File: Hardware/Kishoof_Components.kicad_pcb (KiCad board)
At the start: 2 copper layers, 47 parts, among them U1 STM32H7B0VBTx, U3 TPS561201, U4 LT1117-3.3, U5 TL074, U6 MX25LM51245G

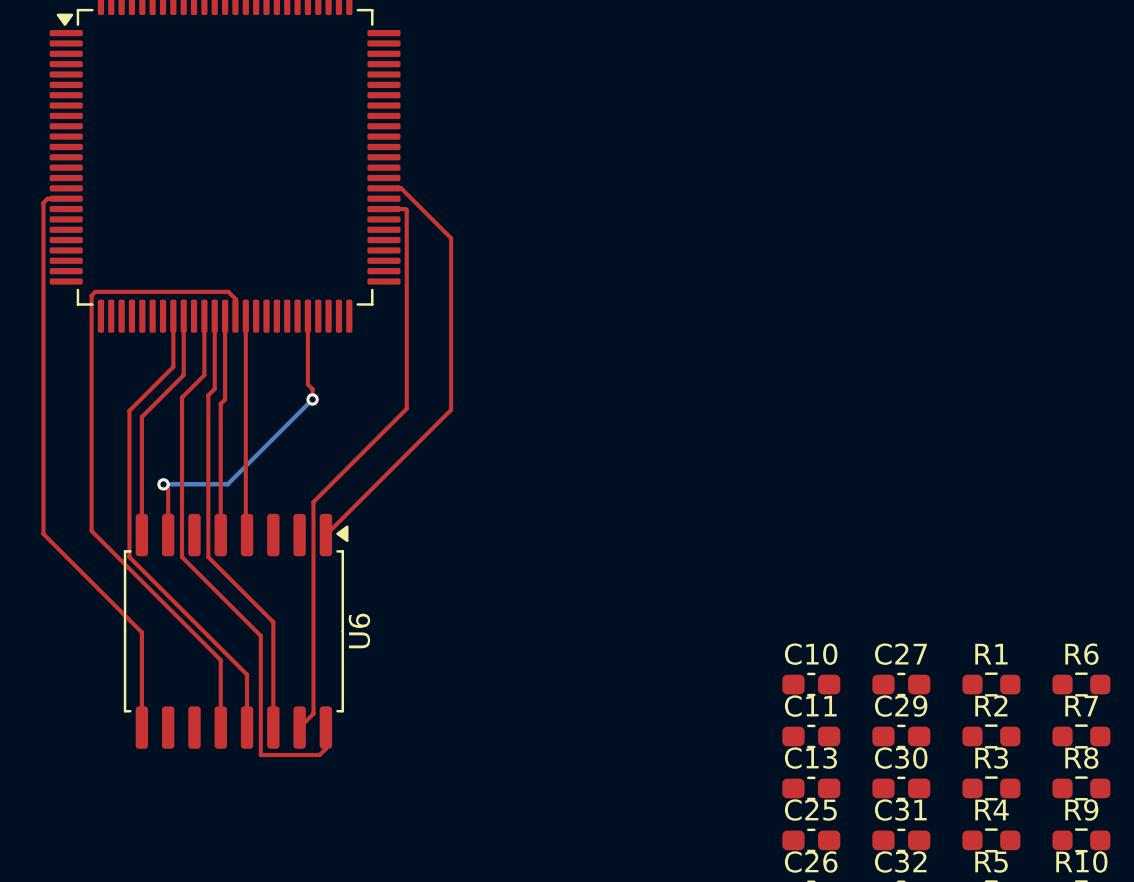
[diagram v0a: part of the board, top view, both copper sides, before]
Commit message: Additional schematic layout
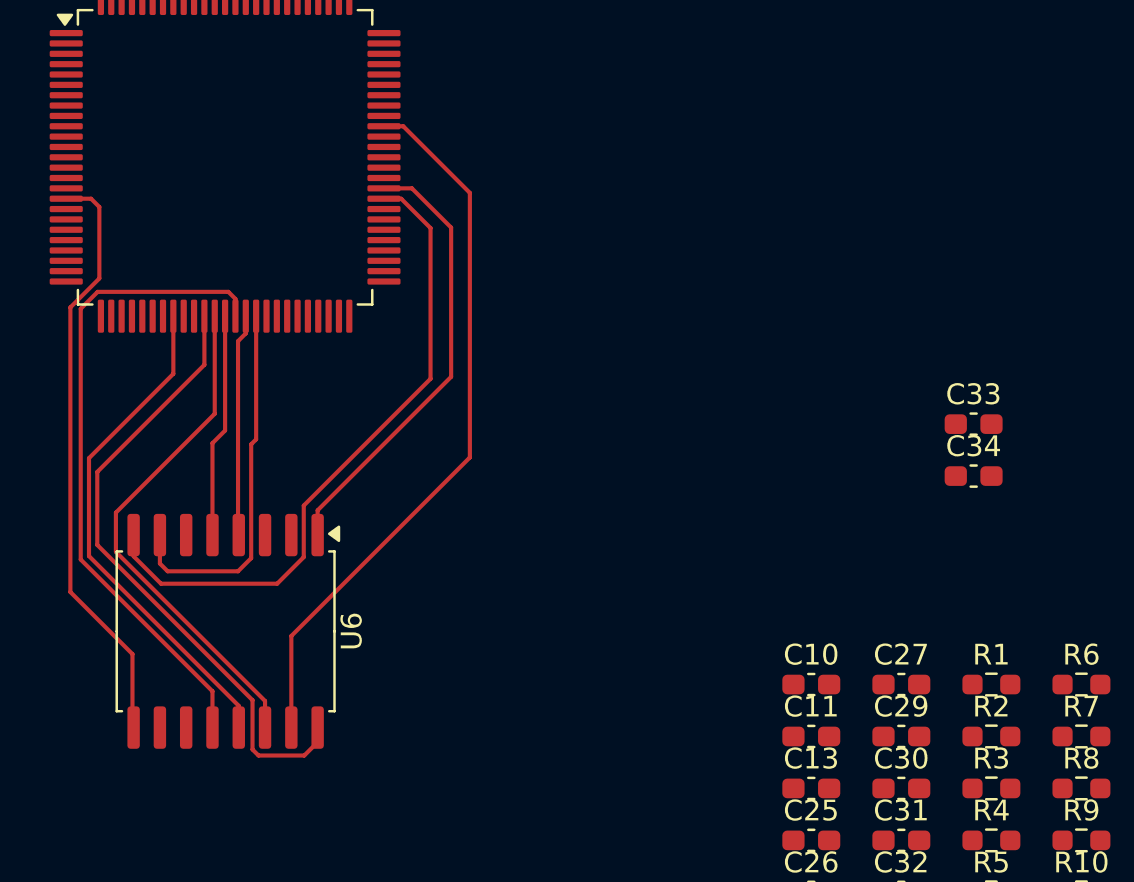
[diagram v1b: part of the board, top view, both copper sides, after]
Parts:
- added C33: 100nF, Capacitor_SMD:C_0603_1608Metric_Pad1.08x0.95mm_HandSolder, F.Cu at (78.9, 71.3)
- added C34: 100nF, Capacitor_SMD:C_0603_1608Metric_Pad1.08x0.95mm_HandSolder, F.Cu at (78.9, 73.8)
- moved U6 0.40 mm to (42.8, 81.3)
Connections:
- U1 pad 1: /OCTOSPIM_P1_IO2 -> unconnected-(U1-PE2-Pad1)
- U1 pad 18: /OCTOSPIM_P1_IO0 -> unconnected-(U1-PC3_C-Pad18)
- U1 pad 23: /OCTOSPIM_P1_DQS -> unconnected-(U1-PA1-Pad23)
- U1 pad 30: /OCTOSPIM_P1_IO3 -> unconnected-(U1-PA6-Pad30)
- U1 pad 34: /OCTOSPIM_P1_IO1 -> unconnected-(U1-PB0-Pad34)
- U1 pad 41: unconnected-(U1-PE11-Pad41) -> /OCTOSPIM_P1_NCS
- U1 pad 58: /OCTOSPIM_P1_IO0 -> unconnected-(U1-PD11-Pad58)
- U1 pad 85: /OCTOSPIM_P1_IO4 -> unconnected-(U1-PD4-Pad85)
- U1 pad 86: /OCTOSPIM_P1_IO5 -> unconnected-(U1-PD5-Pad86)
- U1 pad 87: /OCTOSPIM_P1_IO6 -> unconnected-(U1-PD6-Pad87)
- U1 pad 88: /OCTOSPIM_P1_IO7 -> unconnected-(U1-PD7-Pad88)
- U6 pad 10: unconnected-(U6-GND-Pad10) -> GND
- U6 pad 11: unconnected-(U6-VCC-Pad11) -> +3V3
- U6 pad 2: unconnected-(U6-VCC-Pad2) -> +3V3
- U6 pad 6: unconnected-(U6-GND-Pad6) -> GND
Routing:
- net /OCTOSPIM_P1_IO1: track 11.4 -> 31.6 mm
- net /OCTOSPIM_P1_IO0: track 28.3 -> 34.9 mm
- net /OCTOSPIM_P1_IO4: track 21.3 -> 24.8 mm
- net /OCTOSPIM_P1_CLK: track 27.5 -> 30.4 mm
- net /OCTOSPIM_P1_NCS: track 15.6 -> 18.0 mm, vias 2 -> 0
- net /OCTOSPIM_P1_DQS: track 23.1 -> 24.6 mm

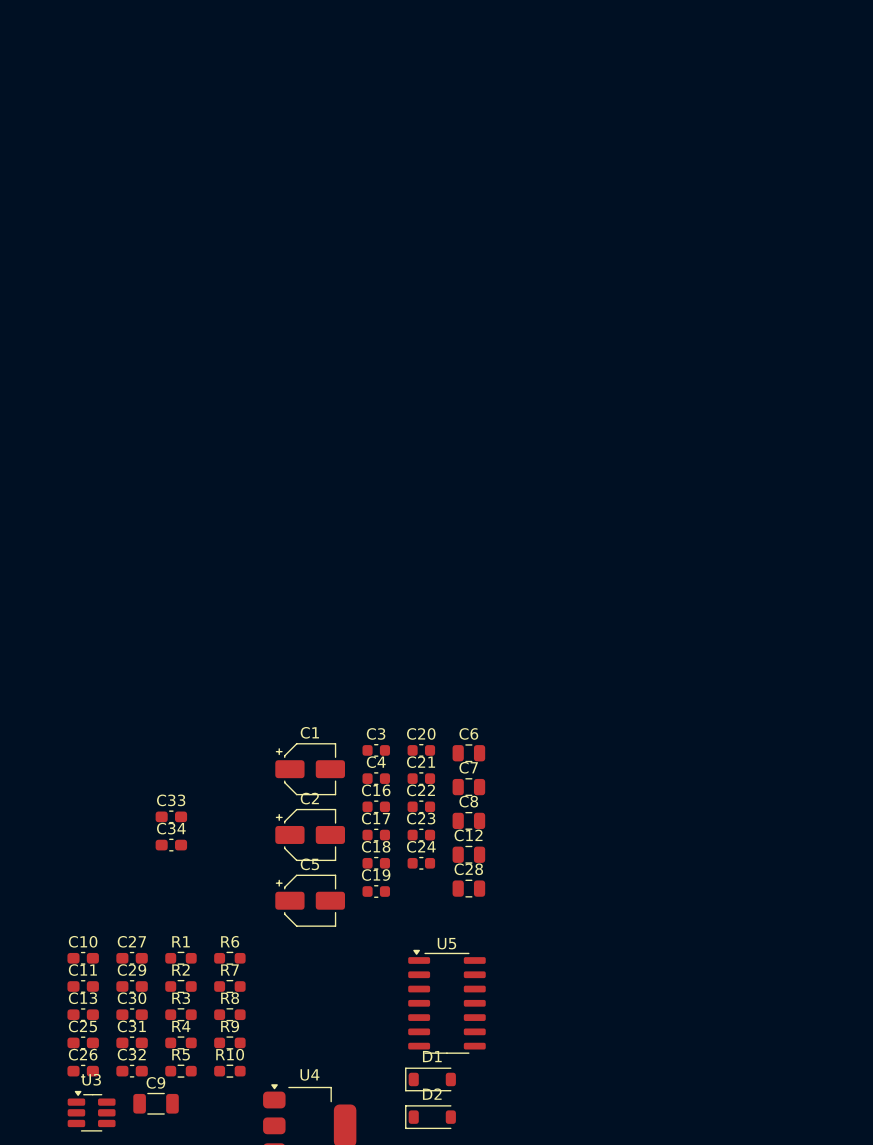
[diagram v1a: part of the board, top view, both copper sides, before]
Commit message: Implemented basic stepped mode for separate wavetables on A and B
Inverted waveform on display
Updates to hardware design
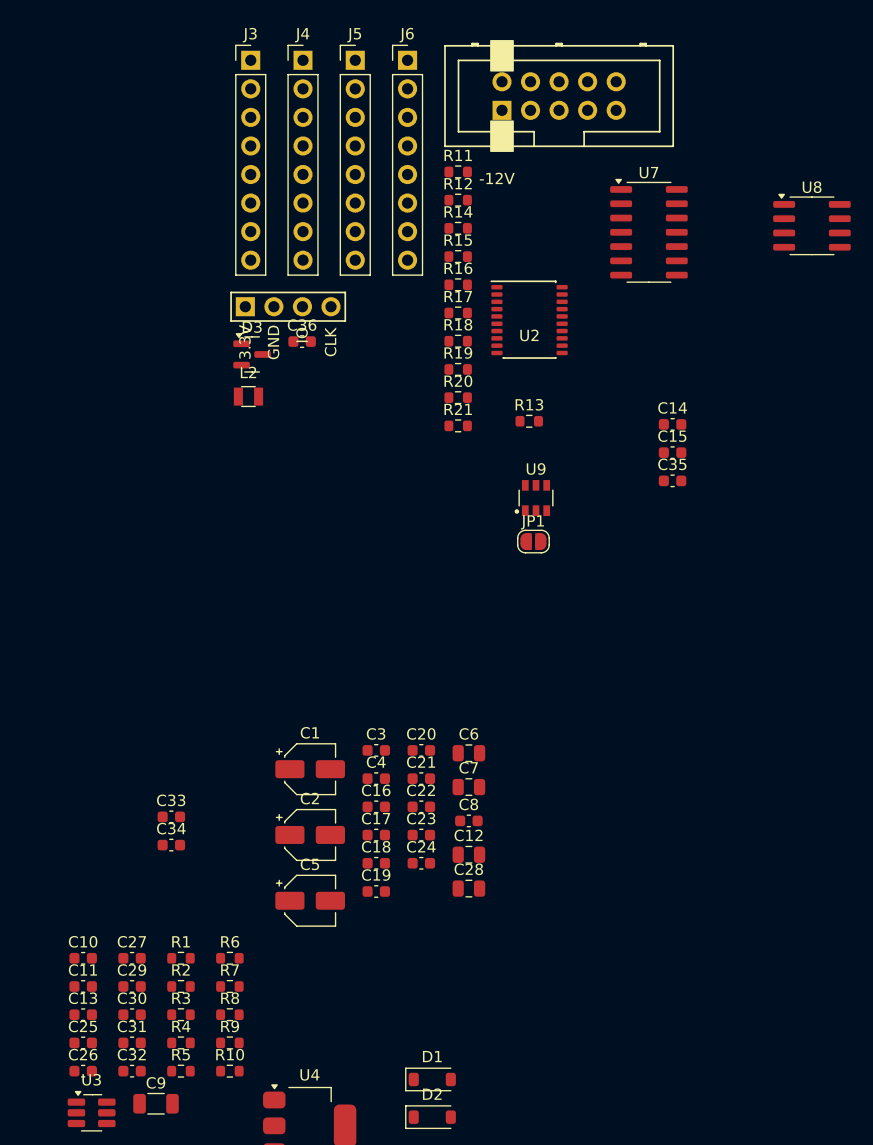
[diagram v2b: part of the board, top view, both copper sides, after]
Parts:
- removed U5: TL074, Package_SO:SOIC-14_3.9x8.7mm_P1.27mm
- added C14: 30pF, Capacitor_SMD:C_0603_1608Metric, F.Cu at (123.5, 36.4)
- added C15: 30pF, Capacitor_SMD:C_0603_1608Metric, F.Cu at (123.5, 38.9)
- added C35: 1.5nF, Capacitor_SMD:C_0603_1608Metric, F.Cu at (123.5, 41.4)
- added C36: 100nF, Capacitor_SMD:C_0603_1608Metric, F.Cu at (90.6, 29.0)
- added D3: LM4040DBZ-5, Package_TO_SOT_SMD:SOT-23, F.Cu at (86.1, 30.2)
- added J1: SWD_Header, Custom_Footprints:SWD_header, F.Cu at (85.5, 25.9)
- added J2: Eurorack_10_pin_power, Custom_Footprints:Eurorack_10_pin_header, F.Cu at (108.3, 8.44)
- added J3: Conn_01x08_Pin, Connector_PinHeader_2.54mm:PinHeader_1x08_P2.54mm_Vertical, F.Cu at (86.0, 3.99)
- added J4: Conn_01x08_Pin, Connector_PinHeader_2.54mm:PinHeader_1x08_P2.54mm_Vertical, F.Cu at (90.7, 3.99)
- added J5: Conn_01x08_Pin, Connector_PinHeader_2.54mm:PinHeader_1x08_P2.54mm_Vertical, F.Cu at (95.3, 3.99)
- added J6: Conn_01x08_Pin, Connector_PinHeader_2.54mm:PinHeader_1x08_P2.54mm_Vertical, F.Cu at (100.0, 3.99)
- added JP1: Jumper, Jumper:SolderJumper-2_P1.3mm_Open_RoundedPad1.0x1.5mm, F.Cu at (111.2, 46.8)
- added L2: 3.3uH, Custom_Footprints:L_0806, F.Cu at (85.8, 33.9)
- added R11: 75k, Resistor_SMD:R_0603_1608Metric, F.Cu at (104.5, 13.9)
- added R12: 91k, Resistor_SMD:R_0603_1608Metric, F.Cu at (104.5, 16.4)
- added R13: 47k, Resistor_SMD:R_0603_1608Metric, F.Cu at (110.8, 36.1)
- added R14: 2k2, Resistor_SMD:R_0603_1608Metric, F.Cu at (104.5, 18.9)
- added R15: 22, Resistor_SMD:R_0603_1608Metric, F.Cu at (104.5, 21.4)
- added R16: 75k, Resistor_SMD:R_0603_1608Metric, F.Cu at (104.5, 24.0)
- added R17: 91k, Resistor_SMD:R_0603_1608Metric, F.Cu at (104.5, 26.5)
- added R18: 75k, Resistor_SMD:R_0603_1608Metric, F.Cu at (104.5, 29.0)
- added R19: 47k, Resistor_SMD:R_0603_1608Metric, F.Cu at (104.5, 31.5)
- added R20: 91k, Resistor_SMD:R_0603_1608Metric, F.Cu at (104.5, 34.0)
- added R21: 47k, Resistor_SMD:R_0603_1608Metric, F.Cu at (104.5, 36.5)
- added U2: PCM5100APW, Custom_Footprints:SSOP-20_4.4x6.5mm_Pitch0.65mm_Round_Pads, F.Cu at (110.8, 27.1)
- added U7: MCP6004, Package_SO:SO-14_3.9x8.65mm_P1.27mm, F.Cu at (121.4, 19.3)
- added U8: TL072, Package_SO:SOIC-8_3.9x4.9mm_P1.27mm, F.Cu at (135.9, 18.7)
- added U9: STF202-22T1G, Custom_Footprints:STF202-22T1G, F.Cu at (111.4, 42.9)
- C10, C11, C13, C25, C26, C27, C29, C30, C31, C32, C33, C34: footprint Capacitor_SMD:C_0603_1608Metric_Pad1.08x0.95mm_HandSolder -> Capacitor_SMD:C_0603_1608Metric
- C8: footprint Capacitor_SMD:C_0805_2012Metric -> Capacitor_SMD:C_0603_1608Metric
- R1, R10, R2, R3, R4, R5, R6, R7, R8, R9: footprint Resistor_SMD:R_0603_1608Metric_Pad0.98x0.95mm_HandSolder -> Resistor_SMD:R_0603_1608Metric
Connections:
- R3 pad 2: /DAC_OUT_L -> /DAC_Out_L
- R4 pad 2: /DAC_OUT_R -> /DAC_Out_R
- U1 pad 22: unconnected-(U1-PA0-Pad22) -> /WAVETABLE_POS_A_POT
- U1 pad 23: unconnected-(U1-PA1-Pad23) -> /WAVETABLE_POS_B_POT
- U1 pad 24: unconnected-(U1-PA2-Pad24) -> /Pitch_CV_Scaled
- U1 pad 25: unconnected-(U1-PA3-Pad25) -> /WaveTable_Pos_A_CV
- U1 pad 28: unconnected-(U1-PA4-Pad28) -> /WaveTable_Pos_B_CV
- U1 pad 63: unconnected-(U1-PC6-Pad63) -> /ENCODER_UP
- U1 pad 64: unconnected-(U1-PC7-Pad64) -> /ENCODER_DN
- U1 pad 65: unconnected-(U1-PC8-Pad65) -> /ENCODER_BTN
- U1 pad 78: /SPI3_SCK -> /LCD_SPI3_SCK
- U1 pad 8: unconnected-(U1-PC14-Pad8) -> /LCD_DC
- U1 pad 80: /SPI3_MOSI -> /LCD_SPI3_MOSI
- U1 pad 9: unconnected-(U1-PC15-Pad9) -> /LCD_RESET
